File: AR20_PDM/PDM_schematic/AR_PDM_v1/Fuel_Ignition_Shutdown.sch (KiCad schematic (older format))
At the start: 24 parts, among them K1 DIPxx-1Cxx-51x, K2 DIPxx-1Cxx-51x, U11 N-MOS, U12 P-MOS, U13 N-MOS, U14 N-MOS, U29 INA233, U30 INA233

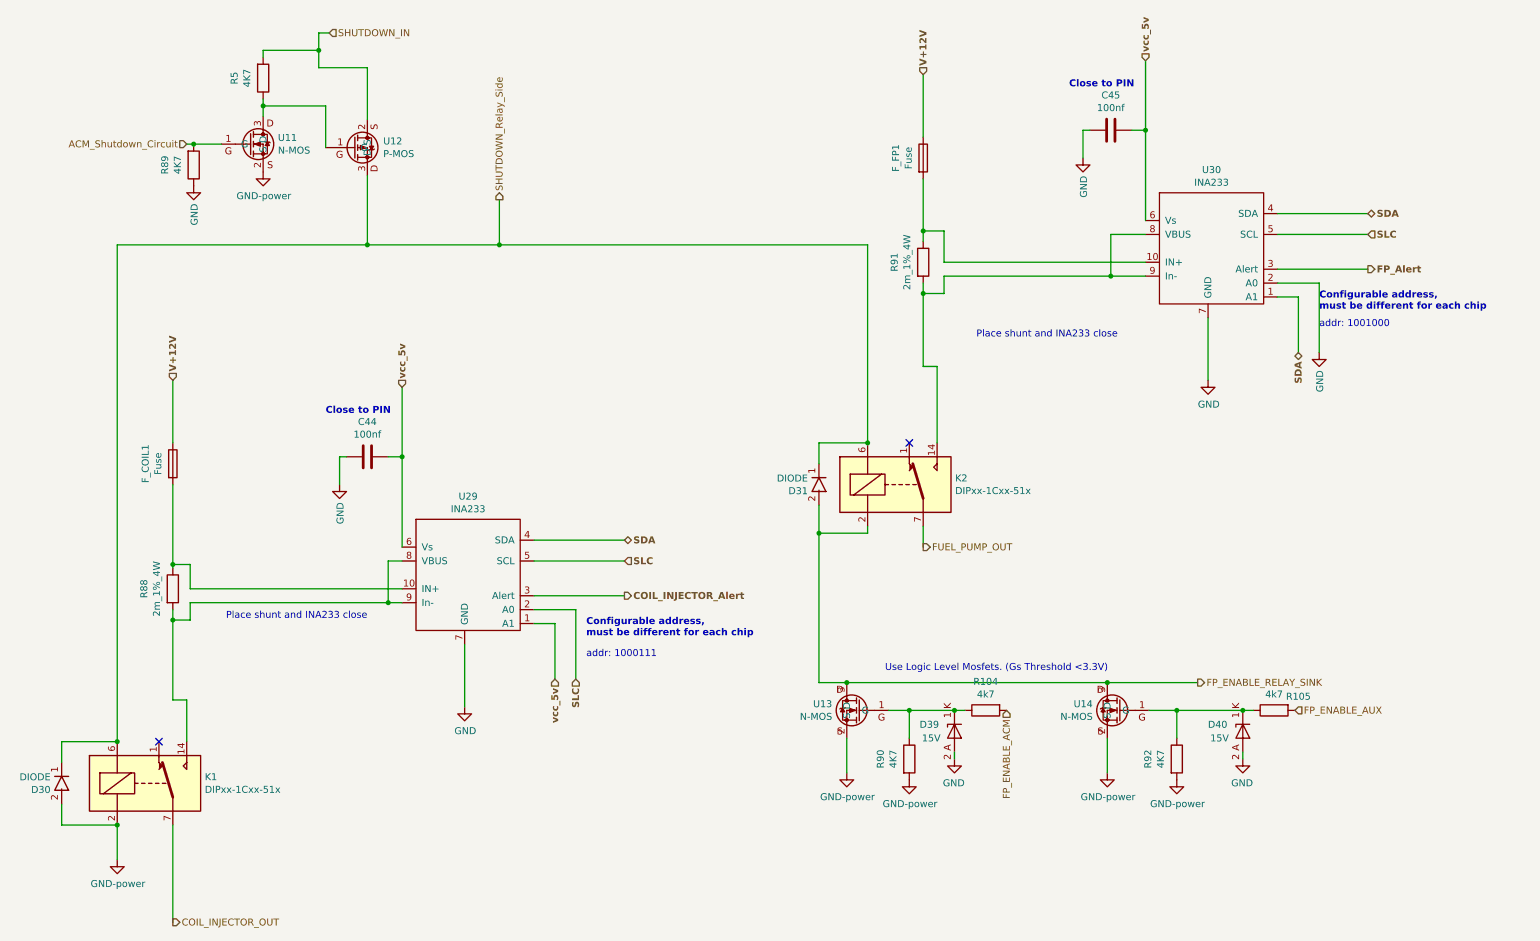
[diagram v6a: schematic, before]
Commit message: Further testing, reveals pdm needs rework
-  As of now, there are major errors in schematics.
- Needs rework. Version charlie postponed.
- Very nice pcb layout thats almost finished. 
   worth noting this layout for the future
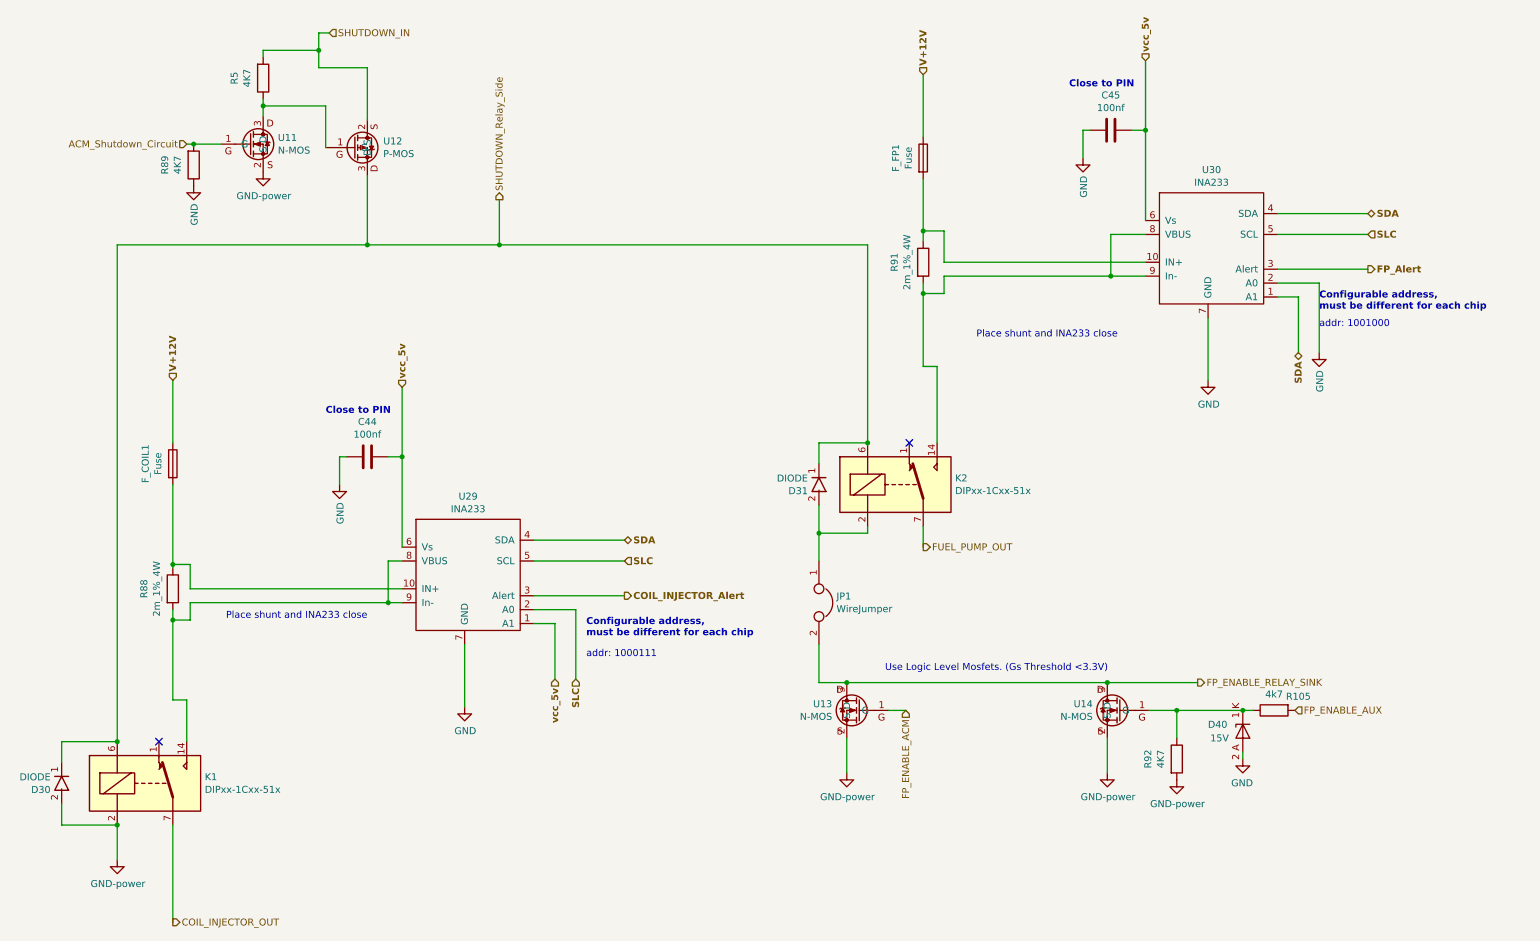
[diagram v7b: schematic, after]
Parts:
- removed D39: 15V, AR_PDM_v1:Diode-BZX585-C15,115, symbol AR20_PDM_v1-rescue:D_Input_protect_zener
- removed R104: 4k7, Resistor_SMD:R_0603_1608Metric, symbol AR20_PDM_v1-rescue:R-Device
- removed R90: 4K7, Resistor_SMD:R_0603_1608Metric, symbol AR20_PDM_v1-rescue:R-Device
- added JP1: WireJumper, AR_PDM_v1:WireJumper_12mm, symbol Device:Jumper
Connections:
- net FP_ENABLE_ACM: now also U13.1 (G)
- net FP_ENABLE_RELAY_SINK: now also JP1.2; no longer D31.2 (A), K2.2
- new net: D31.2 (A), JP1.1, K2.2
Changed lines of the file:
@@
 Wire Wire Line
 	6600 3650 6950 3650
-Wire Wire Line
-	7100 5575 7250 5575
 $Comp
 L AR20_PDM_v1-rescue:GND-power #PWR0118
@@
 Wire Wire Line
 	8675 5775 8675 6025
-$Comp
-L AR20_PDM_v1-rescue:R-Device R?
-U 1 1 5DDC298C
-P 7250 5925
-AR Path="/5DA89415/5DDC298C" Ref="R?"  Part="1"
-AR Path="/5DA8920B/5DDC298C" Ref="R90"  Part="1"
-F 0 "R90" V 7043 5925 50  0000 C CNN
-F 1 "4K7" V 7134 5925 50  0000 C CNN
-F 2 "Resistor_SMD:R_0603_1608Metric" V 7180 5925 50  0001 C CNN
-F 3 "~" H 7250 5925 50  0001 C CNN
-	1    7250 5925
-	1    0    0    -1
-$EndComp
-$Comp
-L AR20_PDM_v1-rescue:GND-power #PWR0119
-U 1 1 5DDC2992
-P 7250 6075
-F 0 "#PWR0119" H 7250 5825 50  0001 C CNN
-F 1 "GND-power" H 7255 5902 50  0000 C CNN
-F 2 "" H 7250 6075 50  0001 C CNN
-F 3 "" H 7250 6075 50  0001 C CNN
-	1    7250 6075
-	1    0    0    -1
-$EndComp
-Wire Wire Line
-	7250 5775 7250 5575
 Wire Wire Line
 	6600 4100 6600 4300
@@
 Wire Wire Line
 	6950 4300 6600 4300
-Connection ~ 6600 4300
 Text HLabel 1950 7100 2    50   Output ~ 0
 COIL_INJECTOR_OUT
@@
 $EndComp
 Wire Wire Line
-	3350 1325 3350 950
-Wire Wire Line
 	3350 950  3000 950
 Wire Wire Line
@@
 FP_ENABLE_RELAY_SINK
 Wire Wire Line
-	6600 4300 6600 5375
-Wire Wire Line
 	7350 1750 7350 2125
 Wire Wire Line
@@
 Wire Wire Line
 	8700 2450 7500 2450
-Wire Wire Line
-	7250 5575 7575 5575
-$Comp
-L AR20_PDM_v1-rescue:R-Device R?
-U 1 1 5E6F759E
-P 7800 5575
-AR Path="/5E5484EE/5E6F759E" Ref="R?"  Part="1"
-AR Path="/5E683DA7/5E6F759E" Ref="R?"  Part="1"
-AR Path="/5DA8920B/5E6F759E" Ref="R104"  Part="1"
-F 0 "R104" V 7593 5575 50  0000 C CNN
-F 1 "4k7" V 7684 5575 50  0000 C CNN
-F 2 "Resistor_SMD:R_0603_1608Metric" V 7730 5575 50  0001 C CNN
-F 3 "" H 7800 5575 50  0001 C CNN
-	1    7800 5575
-	0    -1   1    0
-$EndComp
-Wire Wire Line
-	7575 5575 7650 5575
-Connection ~ 7575 5575
-$Comp
-L AR20_PDM_v1-rescue:D_Input_protect_zener D?
-U 1 1 5E6F7596
-P 7575 5725
-AR Path="/5E683DA7/5E6F7596" Ref="D?"  Part="1"
-AR Path="/5DA8920B/5E6F7596" Ref="D39"  Part="1"
-F 0 "D39" V 7527 5836 50  0000 L CNN
-F 1 "15V" V 7625 5825 50  0000 L CNN
-F 2 "AR_PDM_v1:Diode-BZX585-C15,115" H 7575 5725 50  0001 C CNN
-F 3 "" H 7575 5725 50  0001 C CNN
-	1    7575 5725
-	0    -1   1    0
-$EndComp
-Wire Wire Line
-	7575 5925 7575 5875
-$Comp
-L AR20_PDM_v1-rescue:GND-power #PWR?
-U 1 1 5E6F758F
-P 7575 5925
-AR Path="/5DA89415/5E6F758F" Ref="#PWR?"  Part="1"
-AR Path="/5DEB10A1/5E6F758F" Ref="#PWR?"  Part="1"
-AR Path="/5DEB20EA/5E6F758F" Ref="#PWR?"  Part="1"
-AR Path="/5E0E4725/5E6F758F" Ref="#PWR?"  Part="1"
-AR Path="/5E0E4A93/5E6F758F" Ref="#PWR?"  Part="1"
-AR Path="/5E0E4EB5/5E6F758F" Ref="#PWR?"  Part="1"
-AR Path="/5E0E5304/5E6F758F" Ref="#PWR?"  Part="1"
-AR Path="/5E0E594B/5E6F758F" Ref="#PWR?"  Part="1"
-AR Path="/5E0E607C/5E6F758F" Ref="#PWR?"  Part="1"
-AR Path="/5E0FB5C8/5E6F758F" Ref="#PWR?"  Part="1"
-AR Path="/5E0FBBBD/5E6F758F" Ref="#PWR?"  Part="1"
-AR Path="/5E0FC3A2/5E6F758F" Ref="#PWR?"  Part="1"
-AR Path="/5E0FCFDC/5E6F758F" Ref="#PWR?"  Part="1"
-AR Path="/5E0FDCCC/5E6F758F" Ref="#PWR?"  Part="1"
-AR Path="/5E10174B/5E6F758F" Ref="#PWR?"  Part="1"
-AR Path="/5E5484EE/5E6F758F" Ref="#PWR?"  Part="1"
-AR Path="/5E683DA7/5E6F758F" Ref="#PWR?"  Part="1"
-AR Path="/5DA8920B/5E6F758F" Ref="#PWR071"  Part="1"
-F 0 "#PWR071" H 7575 5675 50  0001 C CNN
-F 1 "GND" H 7580 5752 50  0000 C CNN
-F 2 "" H 7575 5925 50  0001 C CNN
-F 3 "" H 7575 5925 50  0001 C CNN
-	1    7575 5925
-	-1   0    0    -1
-$EndComp
-Text HLabel 7950 5575 3    50   Input ~ 0
+Text HLabel 7225 5575 3    50   Input ~ 0
 FP_ENABLE_ACM
-Connection ~ 7250 5575
 $Comp
 L AR20_PDM_v1-rescue:R-Device R?
@@
 Wire Wire Line
 	9175 5575 9650 5575
+$Comp
+L Device:Jumper JP1
+U 1 1 5E8039E3
+P 6600 4800
+F 0 "JP1" V 6554 4926 50  0000 L CNN
+F 1 "WireJumper" V 6645 4926 50  0000 L CNN
+F 2 "AR_PDM_v1:WireJumper_12mm" H 6600 4800 50  0001 C CNN
+F 3 "~" H 6600 4800 50  0001 C CNN
+	1    6600 4800
+	0    1    1    0
+$EndComp
+Wire Wire Line
+	6600 4500 6600 4300
+Connection ~ 6600 4300
+Wire Wire Line
+	6600 5100 6600 5375
+Wire Wire Line
+	7100 5575 7225 5575
+Wire Wire Line
+	3350 950  3350 1325
 $EndSCHEMATC
